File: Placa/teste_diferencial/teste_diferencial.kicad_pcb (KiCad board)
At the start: 2 copper layers, 50 x 77.6 mm, 32 parts, among them J1 Conn_02x05_Counter_Clockwise, J2 Torque, J3 Tração, J4 ThrottleReceptor, J5 USART_USB, J6 ESC, Q1 AO3401, U1 CH32V003FxPx, U2 ACS758xCB-100U-PFF, U3 LM358, U4 AMS1117-5.0

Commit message: Função do PWM
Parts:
- removed D1: 1N4148W, Diode_SMD:D_SOD-123
- removed D2: LED, LED_THT:LED_D3.0mm
- added Q2: BC547, Package_TO_SOT_THT:TO-92_Inline, F.Cu at (63.7, 110.2)
- moved R6 9.11 mm to (63.0, 102.6)
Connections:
- J5 pad 4: Net-(D1-A) -> +5V
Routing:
- net /I2C_SCL: track 16.7 -> 0.00 mm
- net /I2C_SDA: track 15.4 -> 0.00 mm
- net /Error_Code: track 17.0 -> 7.12 mm
- net Net-(D1-A): track 3.30 -> 0.00 mm
- net +5V: track 44.2 -> 42.9 mm, vias 5 -> 4

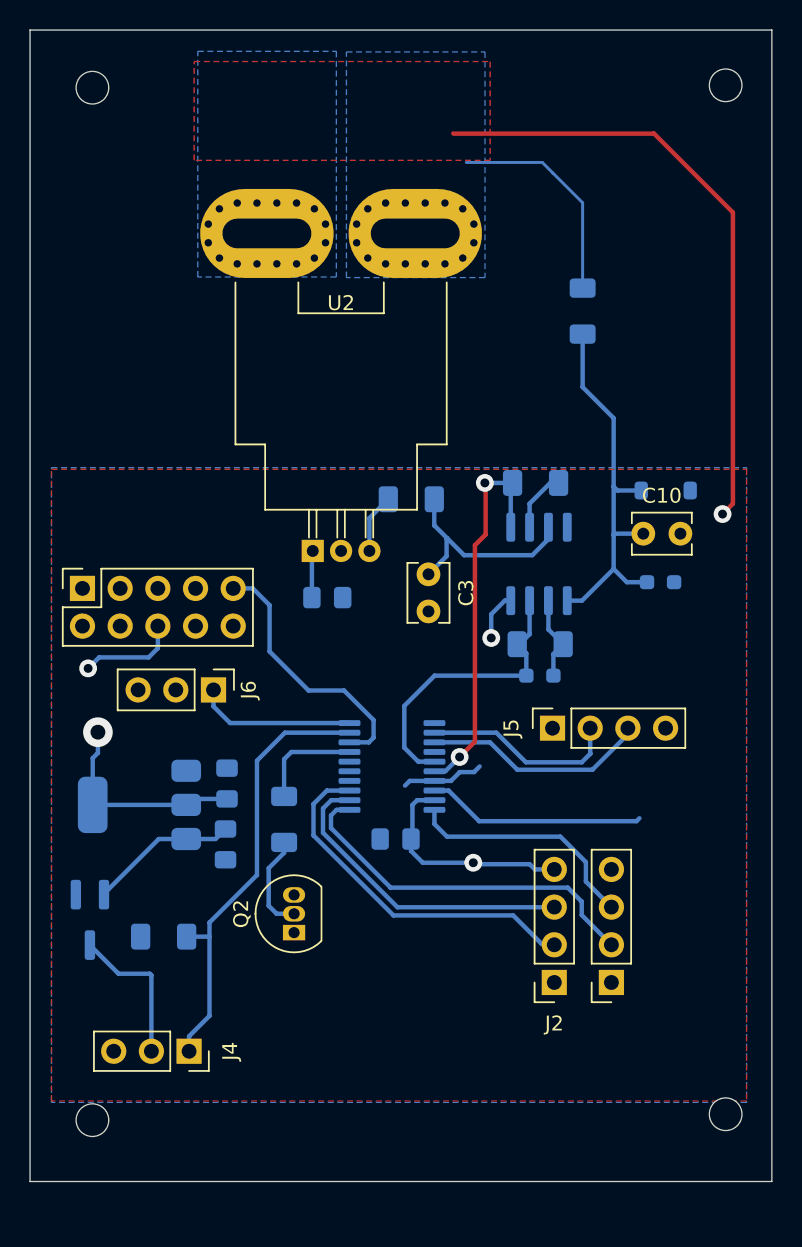
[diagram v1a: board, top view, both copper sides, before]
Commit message: Driver do Timer1 e as funções do som e handler de erro
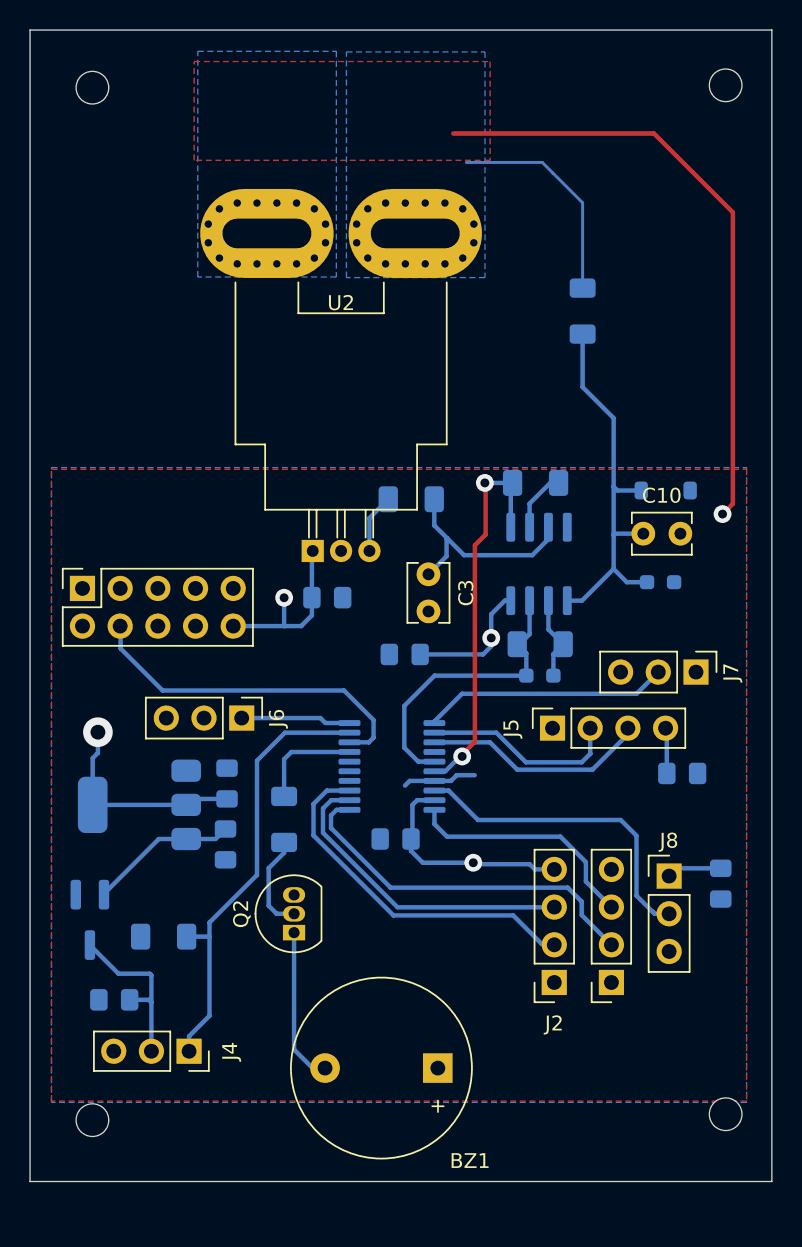
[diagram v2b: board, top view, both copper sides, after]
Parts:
- added BZ1: Buzzer, Buzzer_Beeper:Buzzer_12x9.5RM7.6, F.Cu at (73.4, 119.3)
- added C2: 100n, Capacitor_SMD:C_0805_2012Metric_Pad1.18x1.45mm_HandSolder, B.Cu at (51.6, 114.7)
- added C5: 100n, Capacitor_SMD:C_0805_2012Metric_Pad1.18x1.45mm_HandSolder, B.Cu at (92.5, 106.9)
- added C6: 100n, Capacitor_SMD:C_0805_2012Metric_Pad1.18x1.45mm_HandSolder, B.Cu at (89.9, 99.5)
- added C7: 100n, Capacitor_SMD:C_0805_2012Metric_Pad1.18x1.45mm_HandSolder, B.Cu at (71.2, 91.5)
- added J7: Pitot, Connector_PinHeader_2.54mm:PinHeader_1x03_P2.54mm_Vertical, F.Cu at (90.8, 92.7)
- added J8: RPM, Connector_PinHeader_2.54mm:PinHeader_1x03_P2.54mm_Vertical, F.Cu at (89.0, 106.4)
- moved J6 2.69 mm to (60.2, 95.8)
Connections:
- net /RX_linker renamed /PD5
- J1 pad 10: /SWCLK_linker -> +5V
- J1 pad 2: /TX_linker -> /SWCLK_linker
- J1 pad 3: unconnected-(J1-Pin_3-Pad3) -> /PD6
- J1 pad 4: unconnected-(J1-Pin_4-Pad4) -> /SWDIO_linker
- J1 pad 6: +5V -> GND
- J1 pad 7: /3V3_linker -> unconnected-(J1-Pin_7-Pad7)
- J1 pad 8: GND -> /3V3_linker
- J1 pad 9: /SWDIO_linker -> unconnected-(J1-Pin_9-Pad9)
- R4 pad 2: /ADC_2 -> /ADC_0
- U1 pad 1: unconnected-(U1-PD4-Pad1) -> /ADC_2
- U1 pad 6: /ADC_2 -> /ADC_0
- U3 pad 1: /ADC_2 -> /ADC_0
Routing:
- net /ADC_0: track 0.00 -> 26.4 mm, vias 0 -> 2
- net +5V: track 42.9 -> 57.3 mm
- net Net-(BZ1--): track 0.00 -> 10.5 mm
- net /ADC_2: track 26.3 -> 16.6 mm, vias 2 -> 0
- net /RPM_int: track 14.8 -> 21.6 mm
- net /SWDIO_linker: track 17.9 -> 23.5 mm
- net /ESC_OUT: track 10.7 -> 7.41 mm
- net /V_recep: track 10.1 -> 11.6 mm
- net GND: track 47.2 -> 46.7 mm

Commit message: Iniciando thrustmanager e mudança leve no pcb
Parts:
- removed REF** (x4): MountingHole_2.2mm_M2, MountingHole:MountingHole_2.2mm_M2
- Q2: value BC547 -> BC327
- R6: value 1k -> 10k
- moved C6 39.2 mm to (51.0, 94.0)
- moved J3 18.2 mm to (68.0, 107.5), turned to 90 degrees
- moved J2 13.4 mm to (67.9, 112.2), turned to 90 degrees
- moved J7 7.38 mm to (84.0, 95.5), turned to 0 degrees
- moved C5 7.07 mm to (91.0, 100.0), turned to 90 degrees
- moved C7 6.59 mm to (76.2, 87.2), turned to 90 degrees
- moved Q2 6.20 mm to (61.5, 116.0)
- moved J8 5.98 mm to (88.0, 100.5), turned to 180 degrees
- moved BZ1 5.34 mm to (68.2, 120.5), turned to 0 degrees
- moved C1 5.13 mm to (75.5, 102.5), turned to -90 degrees
- moved J5 1.52 mm to (80.0, 95.4), turned to 0 degrees
- moved R6 1.06 mm to (62.0, 102.5)
- moved R7 0.59 mm to (80.3, 92.3)
- moved R5 0.48 mm to (80.2, 90.3)
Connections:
- BZ1 pad 1: +5V -> Net-(BZ1-+)
- BZ1 pad 2: Net-(BZ1--) -> GND
- Q2 pad 1: Net-(BZ1--) -> Net-(BZ1-+)
- Q2 pad 3: GND -> +5V
- U1 pad 10: /HX711_1_SCK -> unconnected-(U1-PC0-Pad10)
- U1 pad 12: /HX711_2_SCK -> /HX711_1_SCK
- U1 pad 13: /HX711_2_DT -> /HX711_2_SCK
- U1 pad 14: unconnected-(U1-PC4-Pad14) -> /HX711_2_DT
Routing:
- net /HX711_1_DT: track 24.9 -> 6.83 mm
- net +5V: track 57.3 -> 44.6 mm
- net Net-(BZ1--): track 10.5 -> 0.00 mm
- net Net-(BZ1-+): track 0.00 -> 10.0 mm
- net /ADC_0: track 26.4 -> 33.9 mm
- net /USART_RX: track 15.2 -> 8.11 mm
- net /HX711_1_SCK: track 16.0 -> 9.33 mm
- net Net-(Q2-B): track 6.63 -> 13.0 mm
- net /USART_TX: track 13.3 -> 7.32 mm
- net /HX711_2_DT: track 24.2 -> 18.5 mm
- net /ADC_2: track 16.6 -> 11.6 mm
- net /RPM_int: track 21.6 -> 17.0 mm
- net GND: track 46.7 -> 43.4 mm
- net /ADC_1: track 20.1 -> 17.6 mm, vias 0 -> 2
- net /HX711_2_SCK: track 21.4 -> 19.0 mm
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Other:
- board size 50 x 77.6 mm -> 50 x 80 mm

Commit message: otimização de memoria e implementação do tubo de pitot
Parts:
- added R10: 15k, Resistor_SMD:R_1206_3216Metric_Pad1.30x1.75mm_HandSolder, B.Cu at (82.7, 117.5)
- added R11: 36k, Resistor_SMD:R_1206_3216Metric_Pad1.30x1.75mm_HandSolder, B.Cu at (86.6, 111.4)
- added R12: 180k, Resistor_SMD:R_1206_3216Metric_Pad1.30x1.75mm_HandSolder, B.Cu at (83.6, 104.8)
- added R9: 10k, Resistor_SMD:R_1206_3216Metric_Pad1.30x1.75mm_HandSolder, B.Cu at (82.6, 120.0)
- added U5: LM358, Package_SO:SOIC-8_3.9x4.9mm_P1.27mm, B.Cu at (82.5, 111.5)
- R1: value 10k -> 90k
- R2: value 2k -> 10k
- R7: value 2k -> 90k
- moved J7 18.2 mm to (91.1, 112.3)
- moved J8 4.16 mm to (83.9, 101.2)
- moved C5 4.14 mm to (86.9, 100.5)
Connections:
- J7 pad 2: /ADC_2 -> /Pitot
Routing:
- net /Pitot: track 0.00 -> 12.9 mm
- net Net-(U5A-+): track 0.00 -> 10.5 mm
- net /ADC_2: track 11.6 -> 20.8 mm, vias 0 -> 2
- net Net-(U5B--): track 0.00 -> 6.33 mm
- net Net-(U5B-+): track 0.00 -> 6.02 mm
- net /RPM_int: track 17.0 -> 12.8 mm
- net +5V: track 44.6 -> 47.8 mm, vias 4 -> 6
- net GND: track 43.4 -> 45.0 mm
- net /ADC_1: track 17.6 -> 18.3 mm
